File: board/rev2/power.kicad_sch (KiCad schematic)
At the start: 18 parts, among them SW1 MS-22D28-G020, U1 TPD6S300A, U2 TPS62933

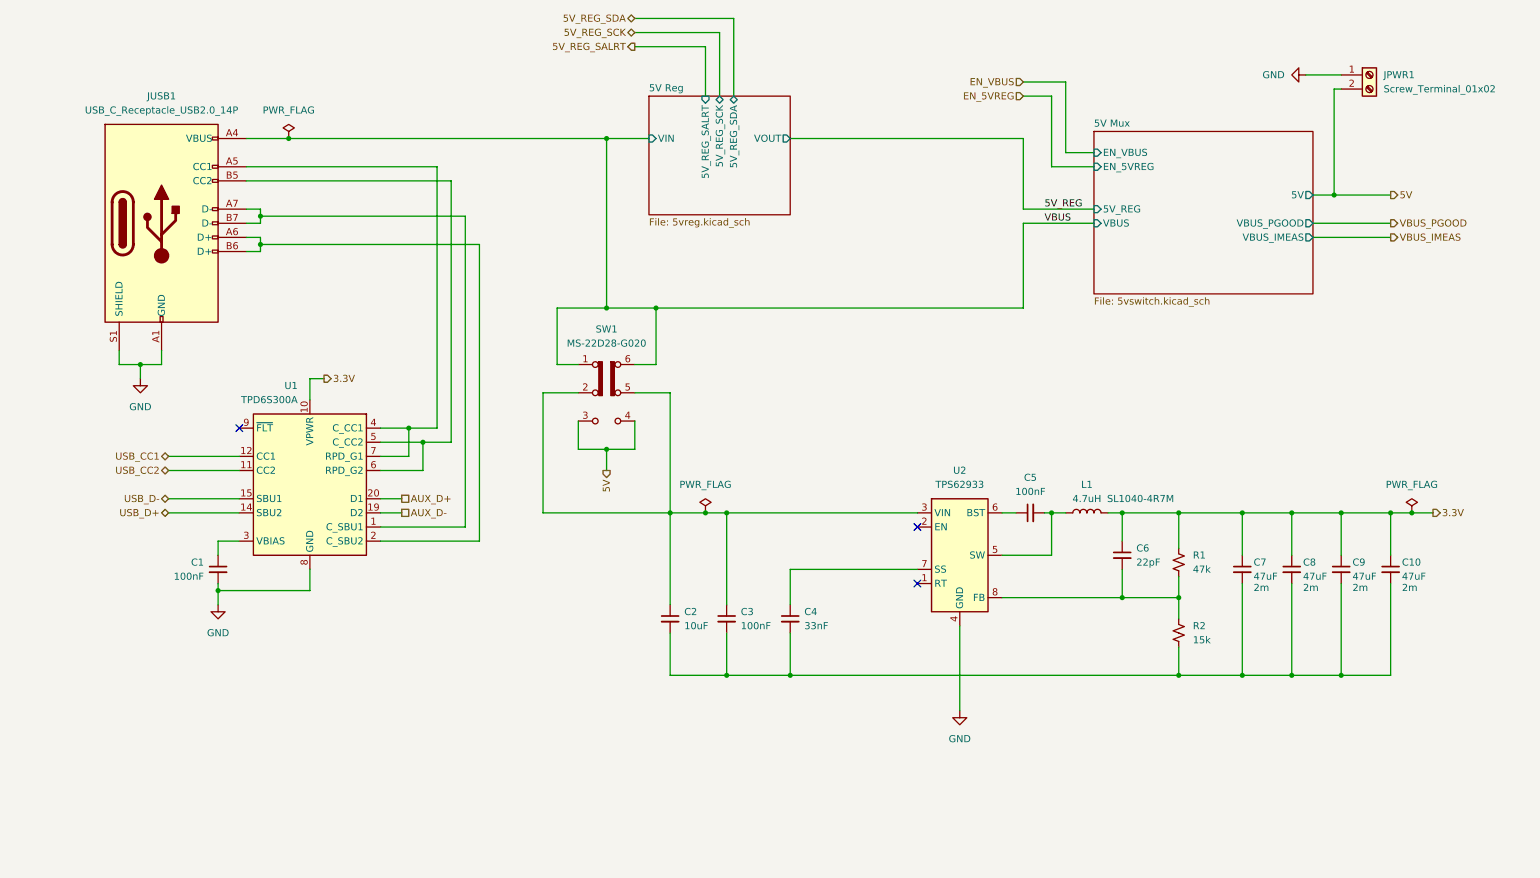
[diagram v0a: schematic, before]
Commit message: More tweaks to schematic, start laying out regulators
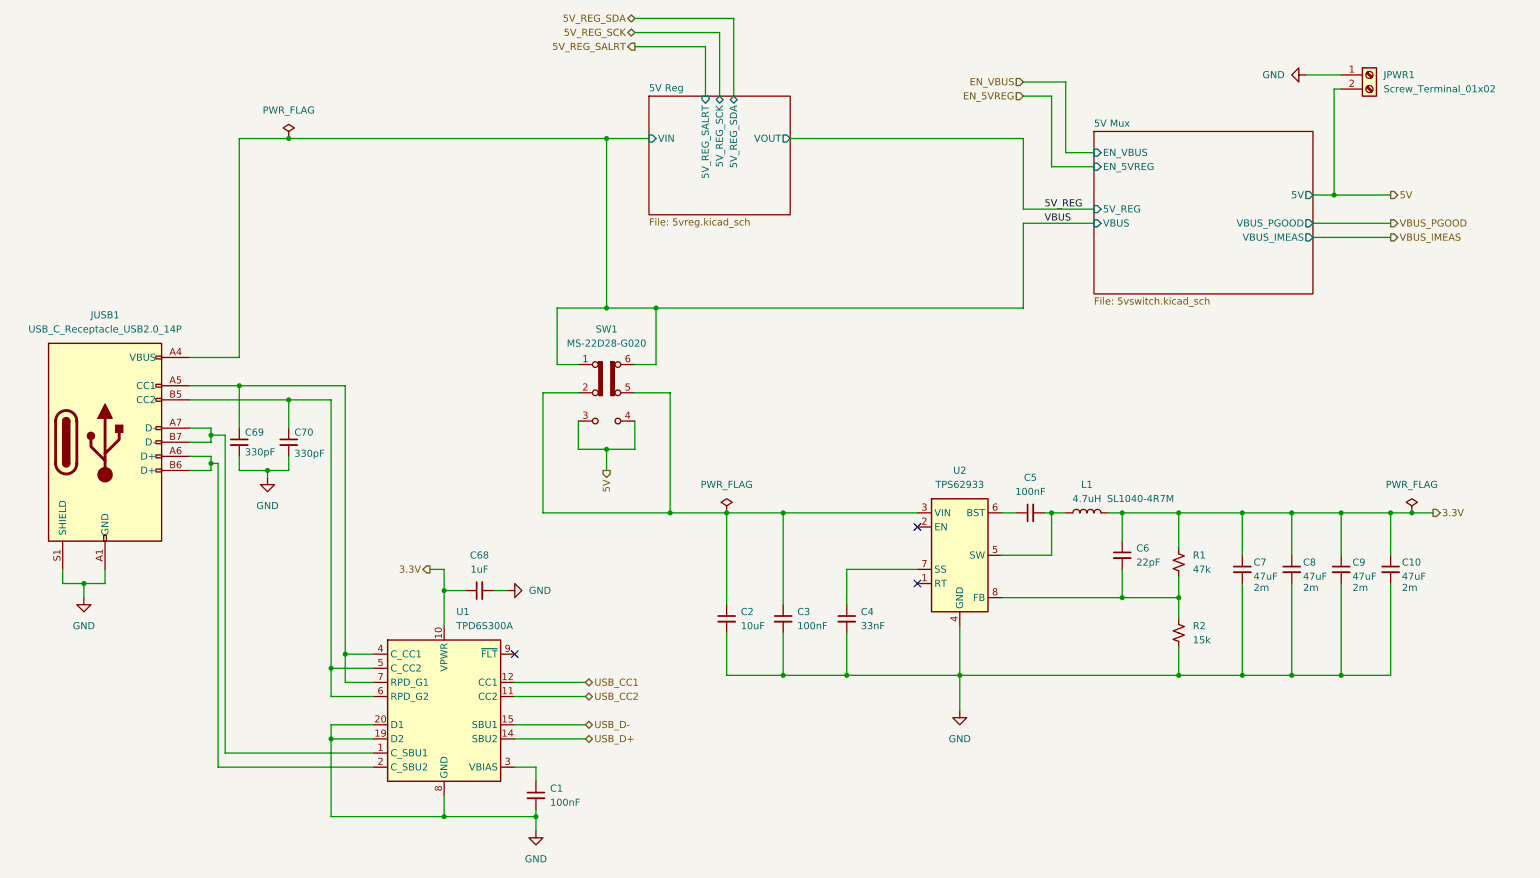
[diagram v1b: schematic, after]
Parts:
- added C68: 1uF, Capacitor_SMD:C_0603_1608Metric, symbol Device:C_Small
- added C69, C70: 330pF, Capacitor_SMD:C_0603_1608Metric, symbol Device:C_Small
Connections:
- net AUX_D+ is gone; now on net GND: U1.20 (D1)
- net AUX_D- is gone; now on net GND: U1.19 (D2)
- net 3.3V: now also C68.1
- net GND: now also C10.2, C2.2, C3.2, C4.2, C7.2, C8.2, C9.2, R2.2, C68.2, C69.2, C70.2
- net at JUSB1.A5 (CC1), U1.4 (C_CC1), U1.7 (RPD_G1): now also C69.1
- net at JUSB1.B5 (CC2), U1.5 (C_CC2), U1.6 (RPD_G2): now also C70.1
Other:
- moved on the sheet: C1, C2, C3, C4, JUSB1, U1

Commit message: 3.3V LDO
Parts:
- added C72: 10uF, Capacitor_SMD:C_1210_3225Metric, symbol Device:C_Small
- added C73: 47uF, Capacitor_SMD:C_1206_3216Metric, symbol Device:C_Small
- added U19: LD1117AG-33-AA3-A-R, Package_TO_SOT_SMD:SOT-223-3_TabPin2, symbol Regulator_Linear:LD1117S33TR_SOT223
- C10: value 47uF -> 10uF; footprint Capacitor_SMD:C_1206_3216Metric -> Capacitor_SMD:C_1210_3225Metric; ESR 2m -> (none); LCSC C96123 -> C13585; Part CL31A476MPHNNNE -> CL31A106KBHNNNE
- C6: value 22pF -> 10pF; footprint Capacitor_SMD:C_0603_1608Metric -> Capacitor_SMD:C_0402_1005Metric; LCSC C1653 -> C32949; Part CL10C220JB8NNNC -> CL05C100JB5NNNC
- L1: value 4.7uH -> 6.8uH; footprint Inductor_SMD:L_TechFuse_SL1040 -> Inductor_SMD:L_Chilisin_BMRF00101040; LCSC C22463838 -> C7502775; Part SL1040-4R7M -> HX CYA1040-6.8UH
- R1: value 47k -> 49.9k; footprint Resistor_SMD:R_0805_2012Metric -> Resistor_SMD:R_0603_1608Metric; LCSC C17713 -> C23184; Part 0805W8F4702T5E -> 0603WAF4992T5E
- R2: value 15k -> 10k; footprint Resistor_SMD:R_0805_2012Metric -> Resistor_SMD:R_0402_1005Metric; LCSC C17475 -> C25744; Part 0805W8F1502T5E -> 0402WGF1002TCE
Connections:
- net 3.3V: now also C72.1, U19.2 (VO); no longer C10.1, C6.1, C7.1, C8.1, C9.1, L1.2, R1.1
- net GND: now also C72.2, C73.2, U19.1 (GND)
- new net: C10.1, C6.1, C7.1, C73.1, C8.1, C9.1, L1.2, R1.1, U19.3 (VI)
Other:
- moved on the sheet: C2, C3, C4, C5, C6, C7, C8, C9, JPWR1, L1, SW1, U2

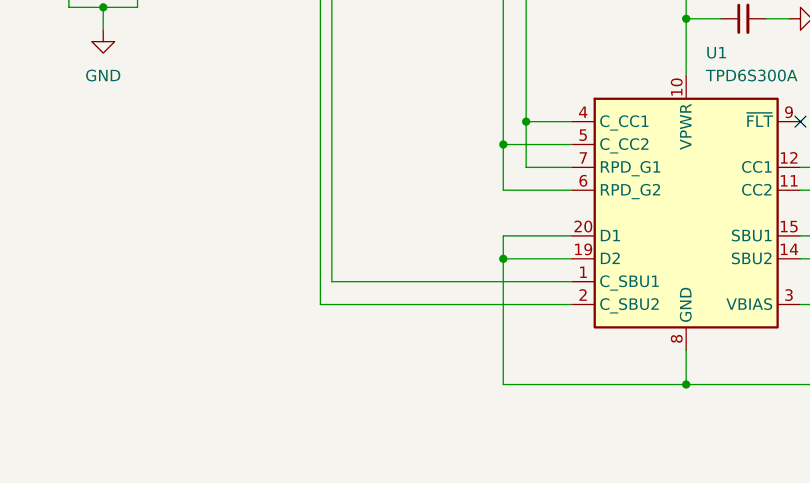
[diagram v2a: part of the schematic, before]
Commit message: Route some more of the board: usb protection / mux
and some of the power mcu
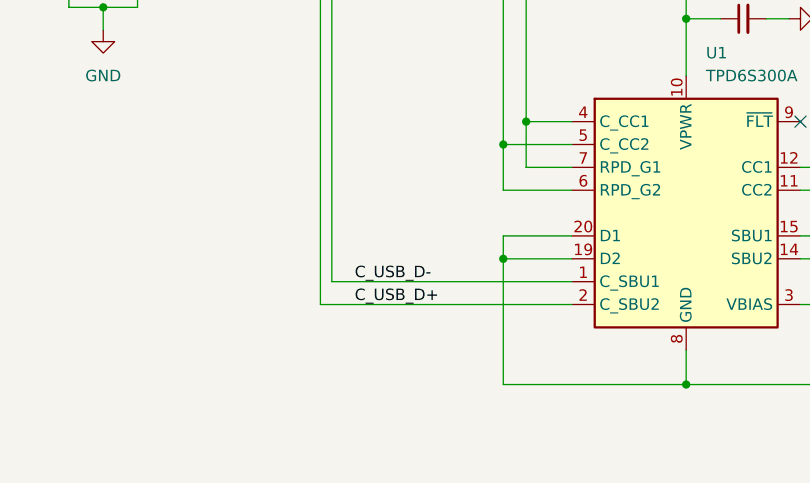
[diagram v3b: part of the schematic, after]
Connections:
- net C_USB_D+: now reaches JUSB1.A6 (D+), JUSB1.B6 (D+), U1.2 (C_SBU2)
- net C_USB_D-: now reaches JUSB1.A7 (D-), JUSB1.B7 (D-), U1.1 (C_SBU1)
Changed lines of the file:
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@@
+		)
+	)
+	(label "C_USB_D+"
+		(at 53.34 163.83 0)
+		(effects
+			(font
+				(size 1.27 1.27)
+			)
+			(justify left bottom)
+		)
+	)
+	(label "C_USB_D-"
+		(at 53.34 161.29 0)
+		(effects
+			(font
+				(size 1.27 1.27)
+			)
+			(justify left bottom)
 		)
 	)

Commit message: Finish board rev2
woo another pcb
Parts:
- added TP1, TP2, TP3, TP4, TP5: TestPoint, TestPoint:TestPoint_Pad_D1.0mm, symbol Connector:TestPoint
- C10, C2, C72: footprint Capacitor_SMD:C_1210_3225Metric -> Capacitor_SMD:C_1206_3216Metric
- JPWR1: footprint TerminalBlock_TE-Connectivity:TerminalBlock_TE_282834-2_1x02_P2.54mm_Horizontal -> Connector_KANGNEX:CONN-TH_4P-P9.50_WJHB9500M-9.5-04P-13-00A; symbol Connector:Screw_Terminal_01x02 -> Connector:Screw_Terminal_01x04
- SW1: value MS-22D28-G020 -> MS-22D17AG2.5-B; footprint Switch_Slide_SMD:SW-SMD_MS-22D28-G020 -> Switch_Slide_SMD:SW-SMD_MS-22D17AG2.5; LCSC C963205 -> C20611671; Part MS-22D28-G020 -> MS-22D17AG2.5-B
- U19: LCSC (none) -> C71121
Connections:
- net 3.3V: now also TP5.1
- net 5V: now also JPWR1.1 (Pin_1)
- net 5V_REG: now also TP3.1
- net GND: now also JPWR1.3 (Pin_3), JPWR1.4 (Pin_4); no longer JPWR1.1 (Pin_1)
- net VBUS: now also TP1.1
- net at C10.1, C6.1, C7.1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: now also TP4.1
- net 3VIN: now reaches C2.1, C3.1, SW1.2 (B), SW1.5 (B), U2.3 (VIN)
- net 3VIN: now also TP2.1

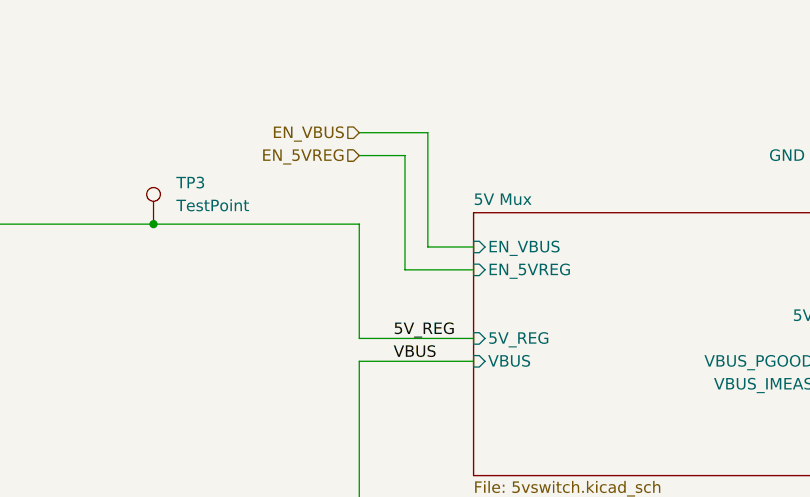
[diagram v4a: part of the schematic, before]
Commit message: Board REVB - fix 5V mux and add discharge path
also, fix a few routing issues
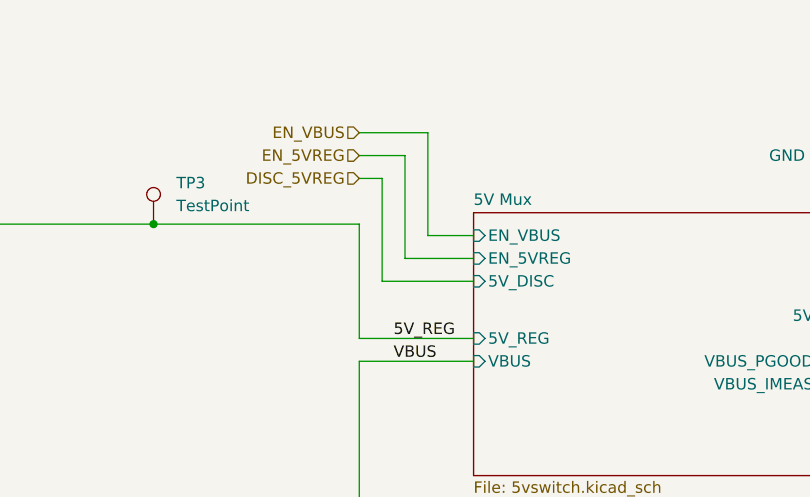
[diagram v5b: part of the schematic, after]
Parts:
- U19: Part (none) -> LD1117AG-33-AA3-A-R
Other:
- sheet 5V Mux ports: added 5V_DISC; removed none
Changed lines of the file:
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@@
 	(wire
 		(pts
+			(xy 187.96 45.72) (xy 190.5 45.72)
+		)
+		(stroke
+			(width 0)
+			(type default)
+		)
+	)
+	(wire
+		(pts
 			(xy 218.44 118.11) (xy 220.98 118.11)
 		)
@@
 	(wire
 		(pts
-			(xy 193.04 43.18) (xy 193.04 55.88)
+			(xy 193.04 43.18) (xy 193.04 54.61)
 		)
 		(stroke
@@
 	(wire
 		(pts
-			(xy 193.04 55.88) (xy 200.66 55.88)
+			(xy 193.04 54.61) (xy 200.66 54.61)
 		)
 		(stroke
@@
 	(wire
 		(pts
+			(xy 200.66 57.15) (xy 190.5 57.15)
+		)
+		(stroke
+			(width 0)
+			(type default)
+		)
+	)
+	(wire
+		(pts
 			(xy 48.26 107.95) (xy 48.26 109.22)
 		)
@@
 	(wire
 		(pts
-			(xy 195.58 53.34) (xy 195.58 40.64)
+			(xy 195.58 52.07) (xy 195.58 40.64)
 		)
 		(stroke
@@
 	(wire
 		(pts
-			(xy 200.66 53.34) (xy 195.58 53.34)
+			(xy 200.66 52.07) (xy 195.58 52.07)
 		)
 		(stroke
@@
 	(wire
 		(pts
+			(xy 190.5 57.15) (xy 190.5 45.72)
+		)
+		(stroke
+			(width 0)
+			(type default)
+		)
+	)
+	(wire
+		(pts
 			(xy 229.87 147.32) (xy 238.76 147.32)
 		)
@@
 		)
 	)
+	(hierarchical_label "DISC_5VREG"
+		(shape input)
+		(at 187.96 45.72 180)
+		(effects
+			(font
+				(size 1.27 1.27)
+			)
+			(justify right)
+		)
+	)
 	(hierarchical_label "5V_REG_SDA"
 		(shape bidirectional)
@@
 			)
 		)
+		(property "Part" "LD1117AG-33-AA3-A-R"
+			(at 261.62 118.11 0)
+			(hide yes)
+			(show_name no)
+			(do_not_autoplace no)
+			(effects
+				(font
+					(size 1.27 1.27)
+				)
+			)
+		)
 		(pin "1"
 		)
@@
 		)
 		(pin "EN_VBUS" input
-			(at 200.66 53.34 180)
+			(at 200.66 52.07 180)
 			(effects
 				(font
@@
 		)
 		(pin "EN_5VREG" input
-			(at 200.66 55.88 180)
+			(at 200.66 54.61 180)
+			(effects
+				(font
+					(size 1.27 1.27)
+				)
+				(justify left)
+			)
+		)
+		(pin "5V_DISC" input
+			(at 200.66 57.15 180)
 			(effects
 				(font
